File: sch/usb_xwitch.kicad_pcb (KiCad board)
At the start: 2 copper layers, 65 x 56.5 mm, 62 parts, among them J1 USB3_A, J2 USB3_A, J3 USB3_A, J4 USB3_A, J5 USB3_A, J6 USB3_A, J7 USB3_A, J8 Conn_02x05_Odd_Even, J9 Conn_02x03_Odd_Even, K1 Relay_DPDT_Panasonic_AGQ200A4H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

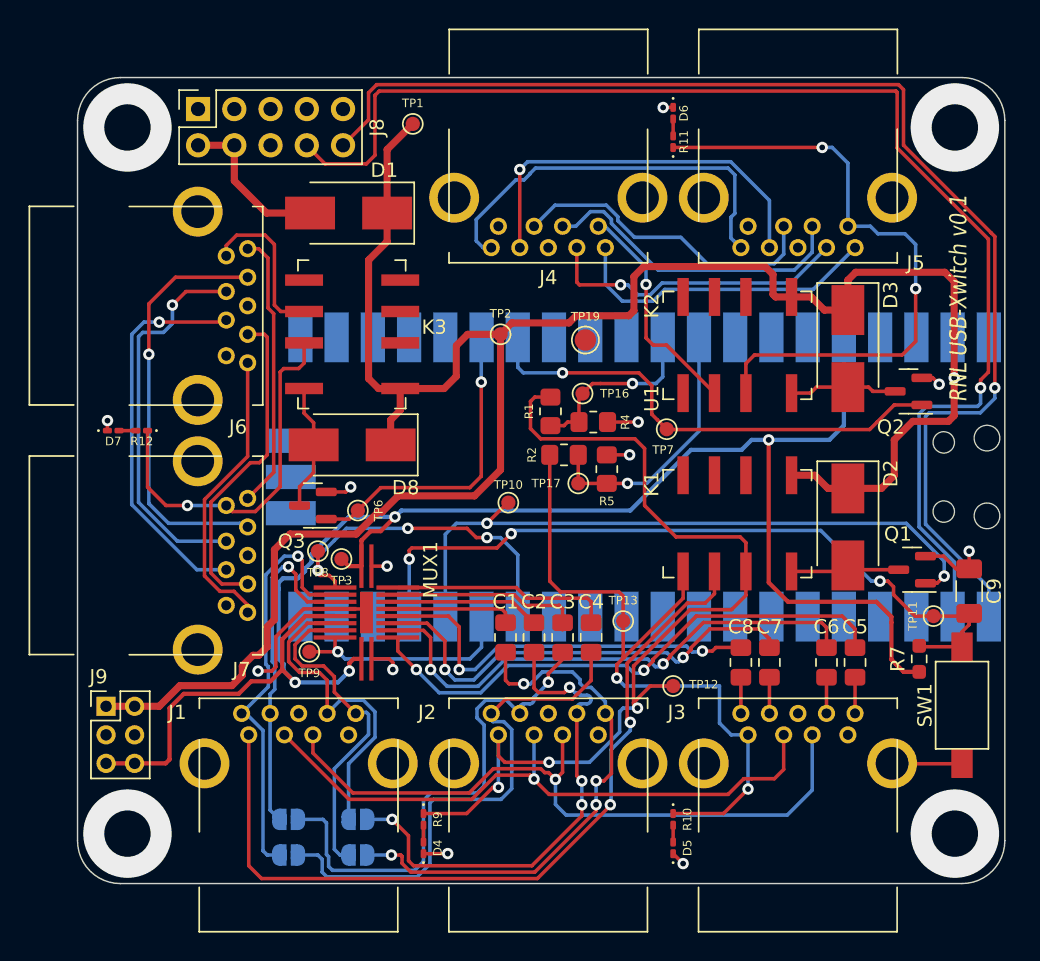
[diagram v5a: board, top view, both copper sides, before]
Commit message: pcb copper poured
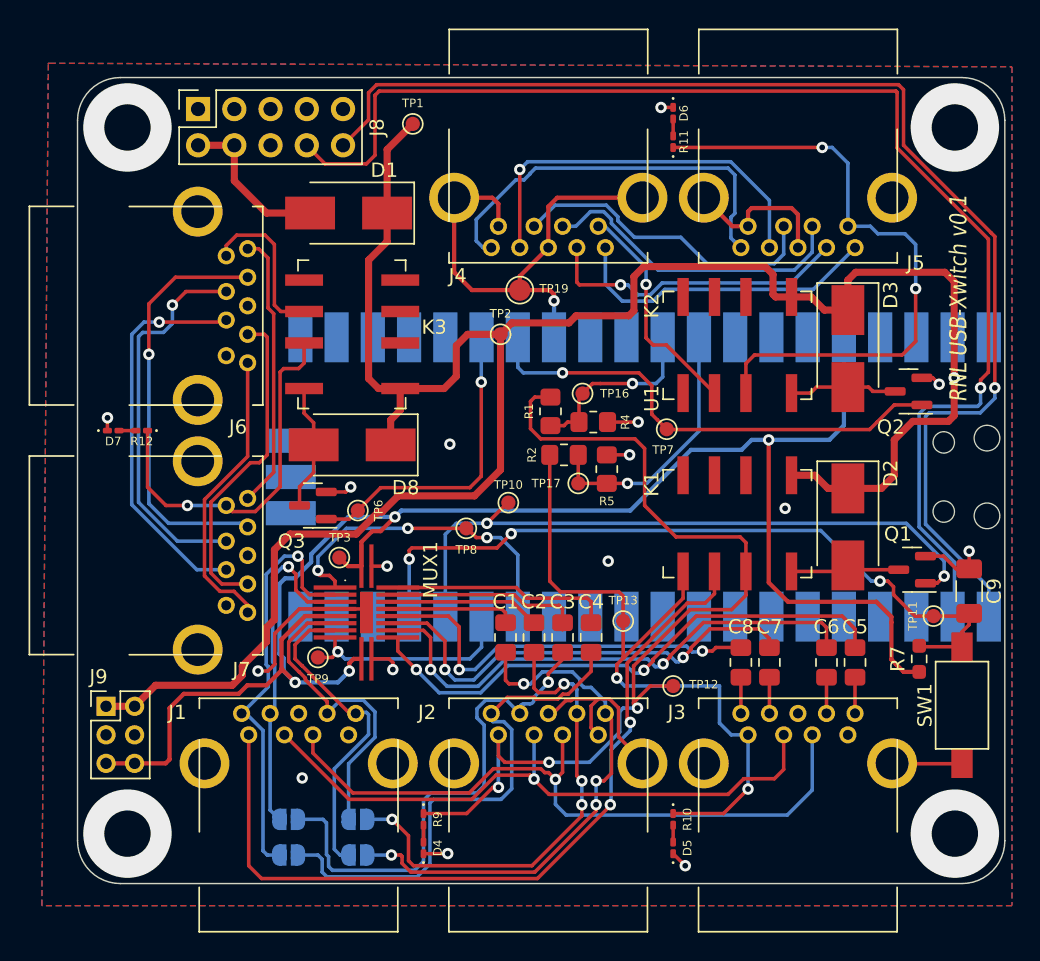
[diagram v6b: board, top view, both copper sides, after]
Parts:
- moved TP8 10.5 mm to (127.2, 111.6)
- moved TP19 5.78 mm to (131.0, 94.9)
- moved TP9 0.72 mm to (116.8, 120.7)
- moved TP3 0.18 mm to (118.3, 113.7)
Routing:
- net GND: track 34.8 -> 94.7 mm, vias 12 -> 17
- net /PD-A: track 23.4 -> 22.1 mm
- net /RX+BP1: track 34.6 -> 33.5 mm
- net /RX+BP: track 23.1 -> 22.3 mm
- net /RX-BP: track 23.3 -> 22.7 mm
- added copper zone on B.Cu, net GND
- added copper zone on F.Cu, net GND

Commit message: updated release and manufacture
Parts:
- added RNL: LOGO, LOGO, F.Cu at (128.4, 104.5)
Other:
- board text added: "JLCJLCJLCJLC"

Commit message: update on new packaging
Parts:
- D4, D5, D6, D7: value LED -> 19-217/GHC-YR1S2/3T; footprint Diode_SMD:D_0201_0603Metric_Pad0.64x0.40mm_HandSolder -> Diode_SMD:D_0603_1608Metric_Pad1.05x0.95mm_HandSolder
- J9: value Conn_02x03_Odd_Even -> C65114; footprint Connector_PinHeader_2.00mm:PinHeader_2x03_P2.00mm_Vertical -> Connector_PinHeader_2.54mm:PinHeader_2x03_P2.54mm_Vertical
- R10, R11, R12, R9: value 402 -> 330Ω; footprint Diode_SMD:D_0201_0603Metric_Pad0.64x0.40mm_HandSolder -> Resistor_SMD:R_0402_1005Metric_Pad0.72x0.64mm_HandSolder
- SW1: value SW_SPST -> C2689642
- moved R9 1.50 mm to (124.2, 130.5)
- moved R11 1.40 mm to (141.8, 85.9)
- moved J9 1.06 mm to (102.2, 123.0)
- moved D5 0.65 mm to (141.8, 134.7)
- moved D4 0.65 mm to (124.2, 133.3)
- moved R12 0.55 mm to (105.0, 104.7)
- moved D6 0.40 mm to (141.8, 82.9)
- moved D7 0.40 mm to (102.1, 104.7)
- moved R10 0.35 mm to (141.8, 131.7)
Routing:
- net Net-(D5-Pad2): track 1.19 -> 2.38 mm, vias 0 -> 1
- net /VBUS2: track 43.8 -> 45.0 mm
- net +5V: track 150.2 -> 149.6 mm
- net GND: track 94.7 -> 94.2 mm, vias 17 -> 16
